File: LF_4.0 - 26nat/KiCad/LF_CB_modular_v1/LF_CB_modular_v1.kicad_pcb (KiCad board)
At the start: 2 copper layers, 60 x 100 mm, 30 parts, among them J1 Conn_QTR16, J10 Conn_01x02, J11 Conn_01x10, J2 Conn_Arducam_MEGA_3mpx, J3 Conn_TB6612FNG_IC, J4 Conn_01x02, J8 Conn_01x01, J9 Conn_01x01, M1 Motor_DC, M2 Motor_DC, Q1 IRF4905, SW1 SW_SPDT, U1 Teensy4.1, U2 LM2940CT-5.0 _TO220

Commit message: getting ready for jlcpcb
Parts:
- removed JW1, JW2: Cam_SCK, Linefollower:Jumper_pin
- removed JW3, JW4: 3V3, Linefollower:Jumper_pin
- added U3: TSR_1-2433, Converter_DCDC:Converter_DCDC_TRACO_TSR-1_THT, F.Cu at (48.6, 119.2)
- moved BT2 1.51 mm to (90.8, 51.6)
- moved C3 1.51 mm to (72.0, 64.2)
- moved D1 1.51 mm to (77.0, 53.2)
- moved R2 1.51 mm to (77.0, 56.2)
- moved R3 1.51 mm to (70.5, 46.8)
- moved R4 1.51 mm to (67.0, 56.2)
- moved SW1 1.51 mm to (85.0, 59.2)
- moved C1 1.51 mm to (58.9, 51.5)
- moved C2 1.51 mm to (45.9, 49.5)
- moved C4 1.51 mm to (56.0, 46.5)
- moved C5 1.51 mm to (51.0, 46.0)
- moved HS1 1.51 mm to (53.5, 61.5)
- moved U2 1.51 mm to (56.0, 54.3)
- moved Q1 1.51 mm to (84.0, 53.3)
- moved R1 1.51 mm to (87.0, 54.6)
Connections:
- J1 pad 3: Net-(JW3-Pin_1) -> /3V3
- J1 pad 4: Net-(JW3-Pin_1) -> /3V3
- J2 pad 3: Net-(J2-SCK) -> /Cam_SCK
- U1 pad 15: /3V3 -> unconnected-(U1-3V3-Pad15)
- U1 pad 35: Net-(JW1-Pin_1) -> /Cam_SCK
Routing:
- net /6V: track 62.1 -> 145.7 mm
- net /Cam_SCK: track 0.00 -> 64.3 mm
- net /5V: track 88.8 -> 50.0 mm
- net /3V3: track 56.3 -> 92.0 mm
- net /BATT_SENSE: track 69.8 -> 75.9 mm
- net Net-(JW3-Pin_1): track 5.74 -> 0.00 mm
- net Net-(JW1-Pin_1): track 2.99 -> 0.00 mm
- net Net-(J2-SCK): track 2.95 -> 0.00 mm
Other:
- board size 60 x 100 mm -> 62 x 100 mm

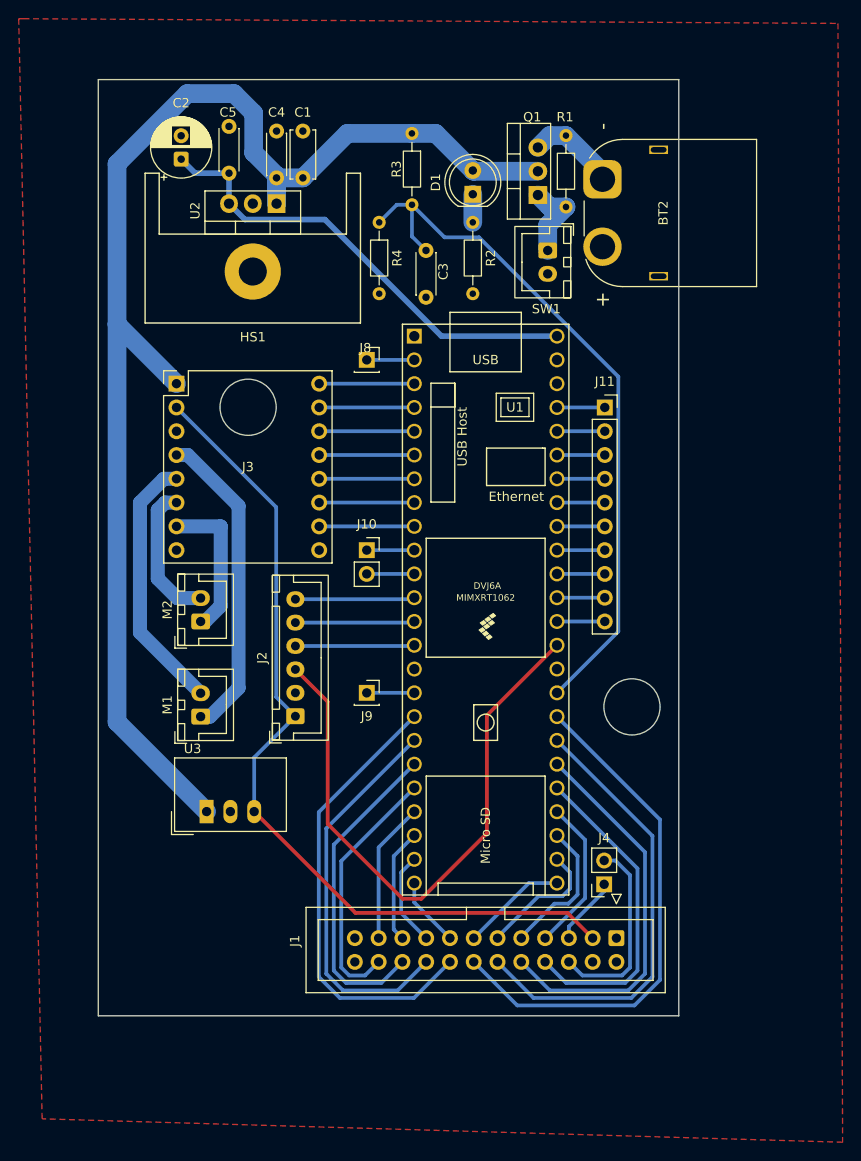
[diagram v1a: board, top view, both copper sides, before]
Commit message: added notes, sedond layer copper mask
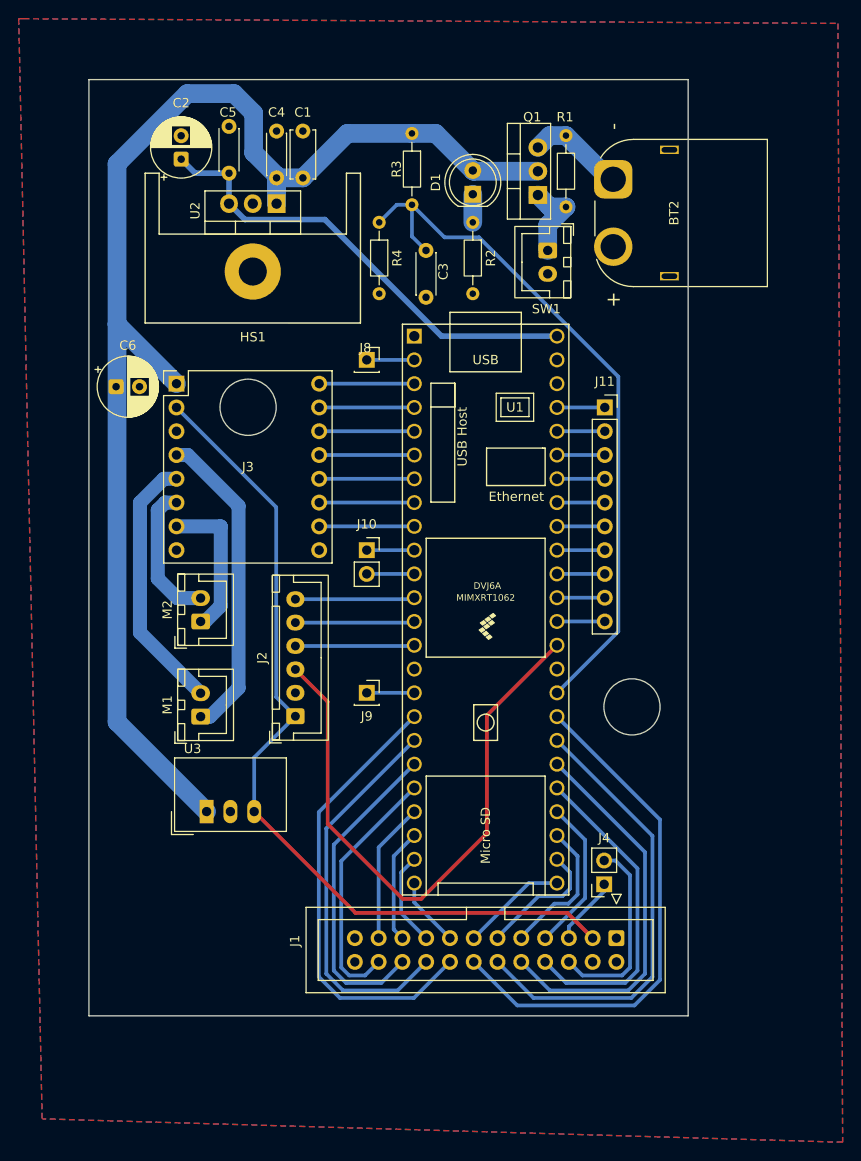
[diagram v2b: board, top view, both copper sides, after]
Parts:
- added C6: C_Polarized_47u, Capacitor_THT:CP_Radial_D6.3mm_P2.50mm, F.Cu at (38.9, 73.8)
- moved BT2 1.15 mm to (92.0, 51.6)
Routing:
- net Net-(BT2-+): track 9.81 -> 10.5 mm
- added copper zone on B.Cu, net /GND
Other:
- board size 62 x 100 mm -> 64 x 100 mm

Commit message: replaced XT60 by wire
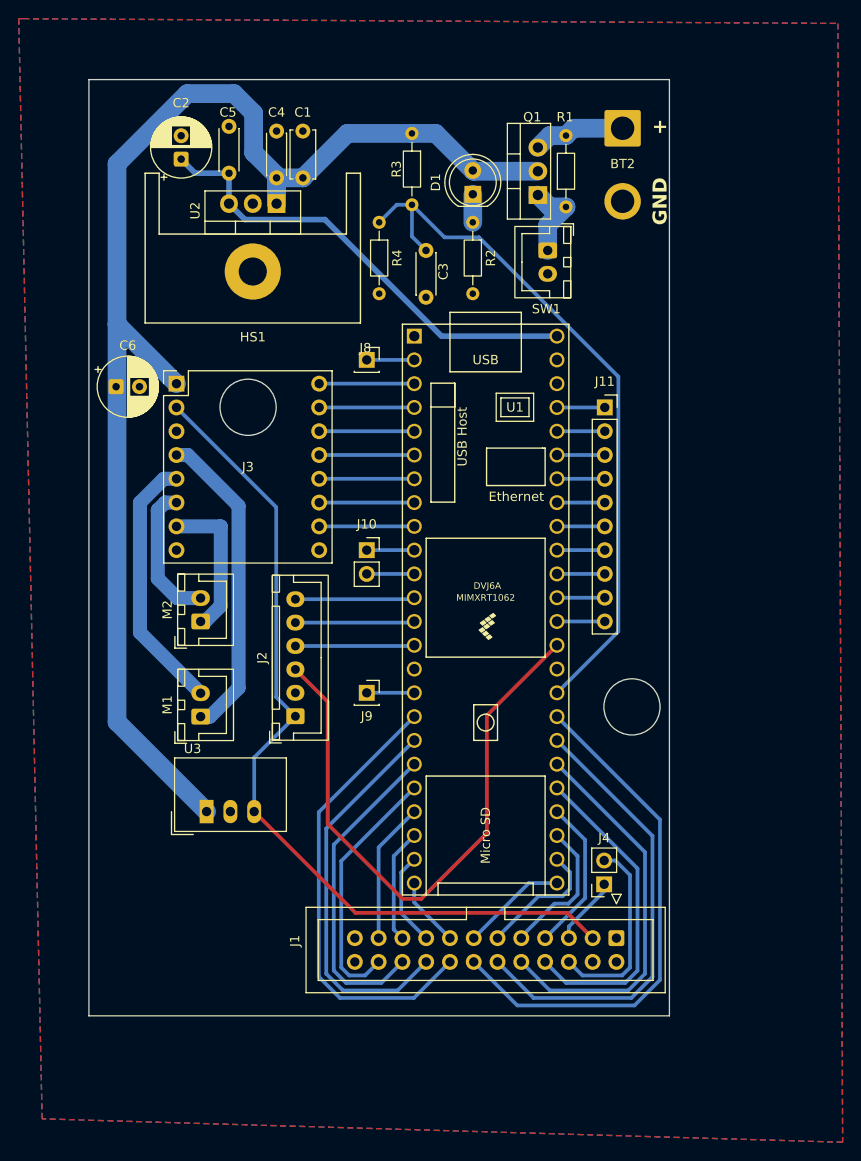
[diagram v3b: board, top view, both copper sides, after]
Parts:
- BT2: footprint Connector_AMASS:AMASS_XT60PW-M_1x02_P7.20mm_Horizontal -> Connector_Wire:SolderWire-2sqmm_1x02_P7.8mm_D2mm_OD3.9mm
- moved BT2 5.54 mm to (93.0, 46.2)
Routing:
- net Net-(BT2-+): track 10.5 -> 9.90 mm
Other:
- board size 64 x 100 mm -> 62 x 100 mm
- board text added: "+"
- board text added: "GND"

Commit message: final. hope so
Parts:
- added J5: Conn_01x05, Connector_PinSocket_2.54mm:PinSocket_1x05_P2.54mm_Vertical, F.Cu at (92.0, 58.9)
- added J6: Conn_01x05, Connector_PinSocket_2.54mm:PinSocket_1x05_P2.54mm_Vertical, F.Cu at (95.6, 58.9)
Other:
- board text added: "Linefollower 4.0 INFIS - ROBO 2026 luksik.j4kub@gmail.com"
- board text added: "Please avoid fire and magic smoke."

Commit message: some last edits
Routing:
- net /3V3: track 92.0 -> 94.5 mm
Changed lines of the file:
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@@
 			)
 		)
+		(model "${KICAD9_3DMODEL_DIR}/Linefollower.3dshapes/Teensy 4.1 (With Headers).step"
+			(offset
+				(xyz 0 0 12)
+			)
+			(scale
+				(xyz 1 1 1)
+			)
+			(rotate
+				(xyz -0 -0 -0)
+			)
+		)
 	)
 	(footprint "Resistor_THT:R_Axial_DIN0204_L3.6mm_D1.6mm_P7.62mm_Horizontal"
@@
 		(tags "Through hole socket strip THT 1x05 2.54mm single row")
 		(property "Reference" "J5"
-			(at 0 -2.77 0)
+			(at 0 12.58 0)
 			(layer "F.SilkS")
 			(effects
@@
 		(tags "Through hole socket strip THT 1x05 2.54mm single row")
 		(property "Reference" "J6"
-			(at 0 -2.77 0)
+			(at 0 12.58 0)
 			(layer "F.SilkS")
 			(effects
@@
 		(model "${KICAD9_3DMODEL_DIR}/LED_THT.3dshapes/LED_D5.0mm.step"
 			(offset
-				(xyz 0 0 0)
+				(xyz 0 0 -3)
 			)
 			(scale
@@
 			)
 			(rotate
-				(xyz 0 0 0)
+				(xyz -0 -0 -0)
 			)
 		)
@@
 		(tags "Through hole socket strip THT 1x01 2.54mm single row")
 		(property "Reference" "J8"
-			(at -0.15 -1.27 0)
+			(at -0.15 -2.44 0)
 			(layer "F.SilkS")
 			(effects
@@
 	)
 	(segment
+		(start 89.8 132.7)
+		(end 89.8 135.24)
+		(width 0.4)
+		(layer "F.Cu")
+		(net 15)
+	)
+	(segment
